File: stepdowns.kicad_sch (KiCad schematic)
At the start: 37 parts, among them J2 12V OUTLET, J3 5V OUTLET, U1 XL7005A, U2 ICW6215, U3 LM1117DT-3.3

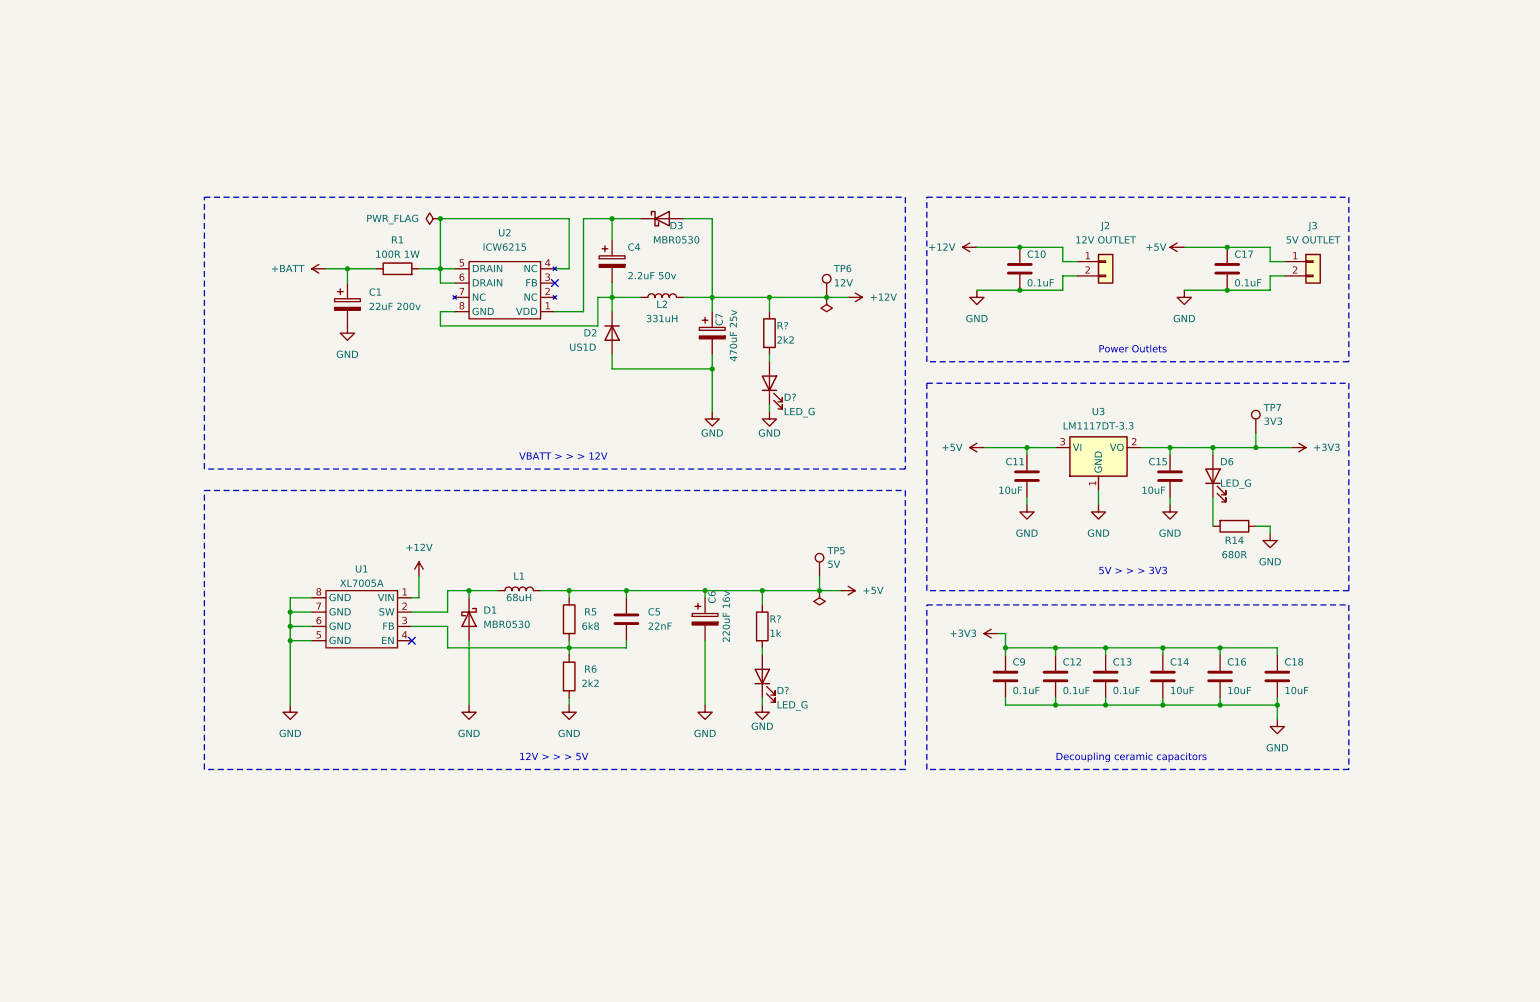
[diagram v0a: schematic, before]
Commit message: Add drivers, stepdown on VIPER115, fixes
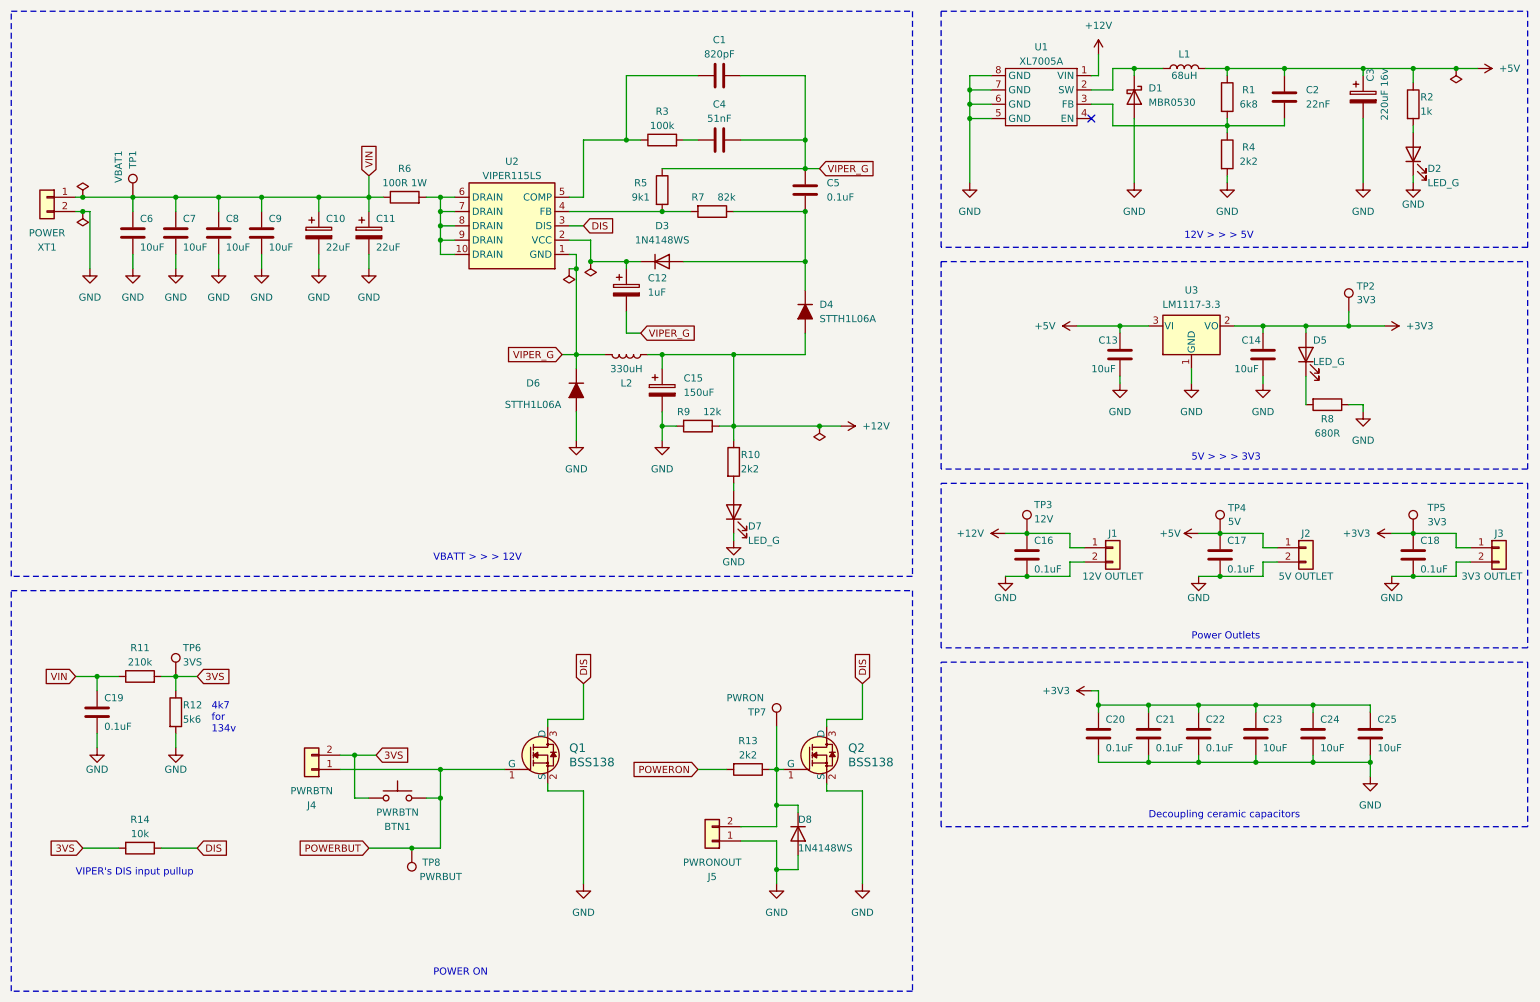
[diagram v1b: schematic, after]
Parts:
- removed C1: 22uF 200v, Capacitor_SMD:CP_Elec_10x10, symbol Device:C_Polarized
- removed C4: 2.2uF 50v, Capacitor_SMD:C_0805_2012Metric_Pad1.18x1.45mm_HandSolder, symbol Device:C_Polarized
- removed C7: 470uF 25v, Capacitor_SMD:CP_Elec_10x10.5, symbol Device:C_Polarized
- removed D2: US1D, Diode_SMD:D_SMA, symbol Diode:US1D
- removed D3: MBR0530, Diode_SMD:D_SOD-123, symbol Diode:MBR0530
- removed D?: LED_G, LED_SMD:LED_0603_1608Metric, symbol Device:LED
- removed R1: 100R 1W, Resistor_SMD:R_2010_5025Metric_Pad1.40x2.65mm_HandSolder, symbol Device:R
- removed R?: 2k2, Resistor_SMD:R_0603_1608Metric_Pad0.98x0.95mm_HandSolder, symbol Device:R
- removed U2: ICW6215, Package_SO:SOP-8_3.9x4.9mm_P1.27mm, symbol 4shift:ICW6215
- removed U3: LM1117DT-3.3, Package_TO_SOT_SMD:TO-252-3_TabPin2, symbol Regulator_Linear:LM1117DT-3.3
- added BTN1: PWRBTN, Button_Switch_SMD:SW_SPST_SKQG_WithoutStem, symbol Switch:SW_Push
- added C1: 820pF, Capacitor_SMD:C_0603_1608Metric_Pad1.08x0.95mm_HandSolder, symbol Device:C
- added C10, C11: 22uF, Capacitor_SMD:CP_Elec_10x10, symbol Device:C_Polarized
- added C12: 1uF, Capacitor_SMD:CP_Elec_10x10, symbol Device:C_Polarized
- added C15: 150uF, Capacitor_SMD:CP_Elec_10x10, symbol Device:C_Polarized
- added C18, C5: 0.1uF, Capacitor_SMD:C_0603_1608Metric_Pad1.08x0.95mm_HandSolder, symbol Device:C
- added C19: 0.1uF, Capacitor_SMD:C_0805_2012Metric_Pad1.18x1.45mm_HandSolder, symbol Device:C
- added C4: 51nF, Capacitor_SMD:C_0603_1608Metric_Pad1.08x0.95mm_HandSolder, symbol Device:C
- added C6, C7, C8, C9: 10uF, Capacitor_SMD:C_0603_1608Metric_Pad1.08x0.95mm_HandSolder, symbol Device:C
- added D3, D8: 1N4148WS, Diode_SMD:D_SOD-323, symbol Diode:1N4148WS
- added D4, D6: STTH1L06A, Diode_SMD:D_SMA_Handsoldering, symbol PCM_Diode_AKL:STTH1L06A
- added D7: LED_G, LED_SMD:LED_0603_1608Metric, symbol Device:LED
- added J3: 3V3 OUTLET, Connector_JST:JST_XH_B2B-XH-A_1x02_P2.50mm_Vertical, symbol Connector_Generic:Conn_01x02
- added J4: PWRBTN, Connector_JST:JST_XH_B2B-XH-A_1x02_P2.50mm_Vertical, symbol Connector_Generic:Conn_01x02
- added J5: PWRONOUT, Connector_JST:JST_XH_B2B-XH-A_1x02_P2.50mm_Vertical, symbol Connector_Generic:Conn_01x02
- added Q1, Q2: BSS138, digikey-footprints:SOT-23-3, symbol dk_Transistors-FETs-MOSFETs-Single:BSS138
- added R10, R13: 2k2, Resistor_SMD:R_0603_1608Metric_Pad0.98x0.95mm_HandSolder, symbol Device:R
- added R11: 210k, Resistor_SMD:R_0805_2012Metric_Pad1.20x1.40mm_HandSolder, symbol Device:R
- added R12: 5k6, Resistor_SMD:R_0805_2012Metric_Pad1.20x1.40mm_HandSolder, symbol Device:R
- added R14: 10k, Resistor_SMD:R_0603_1608Metric_Pad0.98x0.95mm_HandSolder, symbol Device:R
- added R3: 100k, Resistor_SMD:R_0201_0603Metric_Pad0.64x0.40mm_HandSolder, symbol Device:R
- added R5: 9k1, Resistor_SMD:R_0201_0603Metric_Pad0.64x0.40mm_HandSolder, symbol Device:R
- added R6: 100R 1W, Resistor_SMD:R_2010_5025Metric_Pad1.40x2.65mm_HandSolder, symbol Device:R
- added R7: 82k, Resistor_SMD:R_0201_0603Metric_Pad0.64x0.40mm_HandSolder, symbol Device:R
- added R9: 12k, Resistor_SMD:R_0201_0603Metric_Pad0.64x0.40mm_HandSolder, symbol Device:R
- added TP1: VBAT1, TestPoint:TestPoint_Pad_D2.0mm, symbol Connector:TestPoint
- added TP3: 12V, TestPoint:TestPoint_Pad_D2.0mm, symbol Connector:TestPoint
- added TP4: 5V, TestPoint:TestPoint_Pad_D2.0mm, symbol Connector:TestPoint
- added TP7: PWRON, TestPoint:TestPoint_Pad_D2.0mm, symbol Connector:TestPoint
- added TP8: PWRBUT, TestPoint:TestPoint_Pad_D2.0mm, symbol Connector:TestPoint
- added U2: VIPER115LS, 4shift:SOIC100P600X175-10N, symbol 4shift:VIPER115LSTR
- added U3: LM1117-3.3, Package_TO_SOT_SMD:SOT-223, symbol Regulator_Linear:LM1117-3.3
- added XT1: POWER, Connector_AMASS:AMASS_XT30PW-M_1x02_P2.50mm_Horizontal, symbol Connector_Generic:Conn_01x02
- J1: renamed from J2; footprint (none) -> Connector_JST:JST_XH_B2B-XH-A_1x02_P2.50mm_Vertical
- J2: renamed from J3; footprint (none) -> Connector_JST:JST_XH_B2B-XH-A_1x02_P2.50mm_Vertical
- L2: value 331uH -> 330uH
- TP5: value 5V -> 3V3
- TP6: value 12V -> 3VS
- gave numbers to parts that had none: 2
- renumbered C11 to C13, C15 to C14, C10 to C16, C5 to C2, C9 to C20, C12 to C21, C13 to C22, C14 to C23, C16 to C24, C18 to C25, C6 to C3, D6 to D5, R5 to R1, R6 to R4, R14 to R8, TP7 to TP2
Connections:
- net +12V: now also C15.1, D4.2 (A), R10.1, R9.1, TP3.1; no longer TP6.1
- net +3V3: now also TP5.1, C18.1, J3.1 (Pin_1), U3.2 (VO)
- net +5V: now also TP4.1, U3.3 (VI); no longer TP5.1
- net GND: now also C10.2, C11.2, C15.2, C18.2, C19.2, C6.2, C7.2, C8.2, C9.2, D6.2 (A), D7.1 (K), D8.2 (A), J3.2 (Pin_2), J5.1 (Pin_1), Q1.2 (S), Q2.2 (S), R12.2, R9.2, U3.1 (GND), XT1.2 (Pin_2)
- net VIPER_G: now reaches L2.1
- net VIPER_G: now also C1.2, C12.2, C4.2, C5.2, D6.1 (K), R5.1, U2.1 (GND)
- new net: R6.2, U2.10 (DRAIN), U2.6 (DRAIN), U2.7 (DRAIN), U2.8 (DRAIN), U2.9 (DRAIN)
- new net: D7.2 (A), R10.2
- new net: D8.1 (K), J5.2 (Pin_2), Q2.1 (G), R13.1, TP7.1
- new net: C12.1, D3.1 (K), U2.2 (VCC)
- new net: R5.2, R7.2, U2.4 (FB)
- new net: C1.1, R3.1, U2.5 (COMP)
- new net: C5.1, D3.2 (A), D4.1 (K), R7.1
- new net: C4.1, R3.2
- new net 3VS: BTN1.1, J4.2 (Pin_2), R11.2, R12.1, R14.2, TP6.1
- new net DIS: Q1.3 (D), Q2.3 (D), R14.1, U2.3 (DIS)
- new net POWERBUT: BTN1.2, J4.1 (Pin_1), Q1.1 (G), TP8.1
- new net POWERON: R13.2
- new net VIN: C10.1, C11.1, C19.1, C6.1, C7.1, C8.1, C9.1, R11.1, R6.1, TP1.1, XT1.1 (Pin_1)
- no-connect marks 2 -> 1
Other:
- note added: "4k7 for 134v"
- note added: "POWER ON"
- note added: "VIPER's DIS input pullup"
- moved on the sheet: C13, C14, C16, C17, C2, C20, C21, C22, C23, C24, C25, C3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

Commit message: topology in progress
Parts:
- C14: footprint Capacitor_SMD:C_0805_2012Metric -> Capacitor_SMD:C_0603_1608Metric_Pad1.08x0.95mm_HandSolder
- R3, R5, R7, R9: footprint Resistor_SMD:R_0201_0603Metric_Pad0.64x0.40mm_HandSolder -> Resistor_SMD:R_0603_1608Metric_Pad0.98x0.95mm_HandSolder
- R8: footprint Resistor_SMD:R_0402_1005Metric -> Resistor_SMD:R_0603_1608Metric_Pad0.98x0.95mm_HandSolder
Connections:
- net GND: now also XT1.1 (Pin_1); no longer XT1.2 (Pin_2)
- net VIN: now also XT1.2 (Pin_2); no longer XT1.1 (Pin_1)

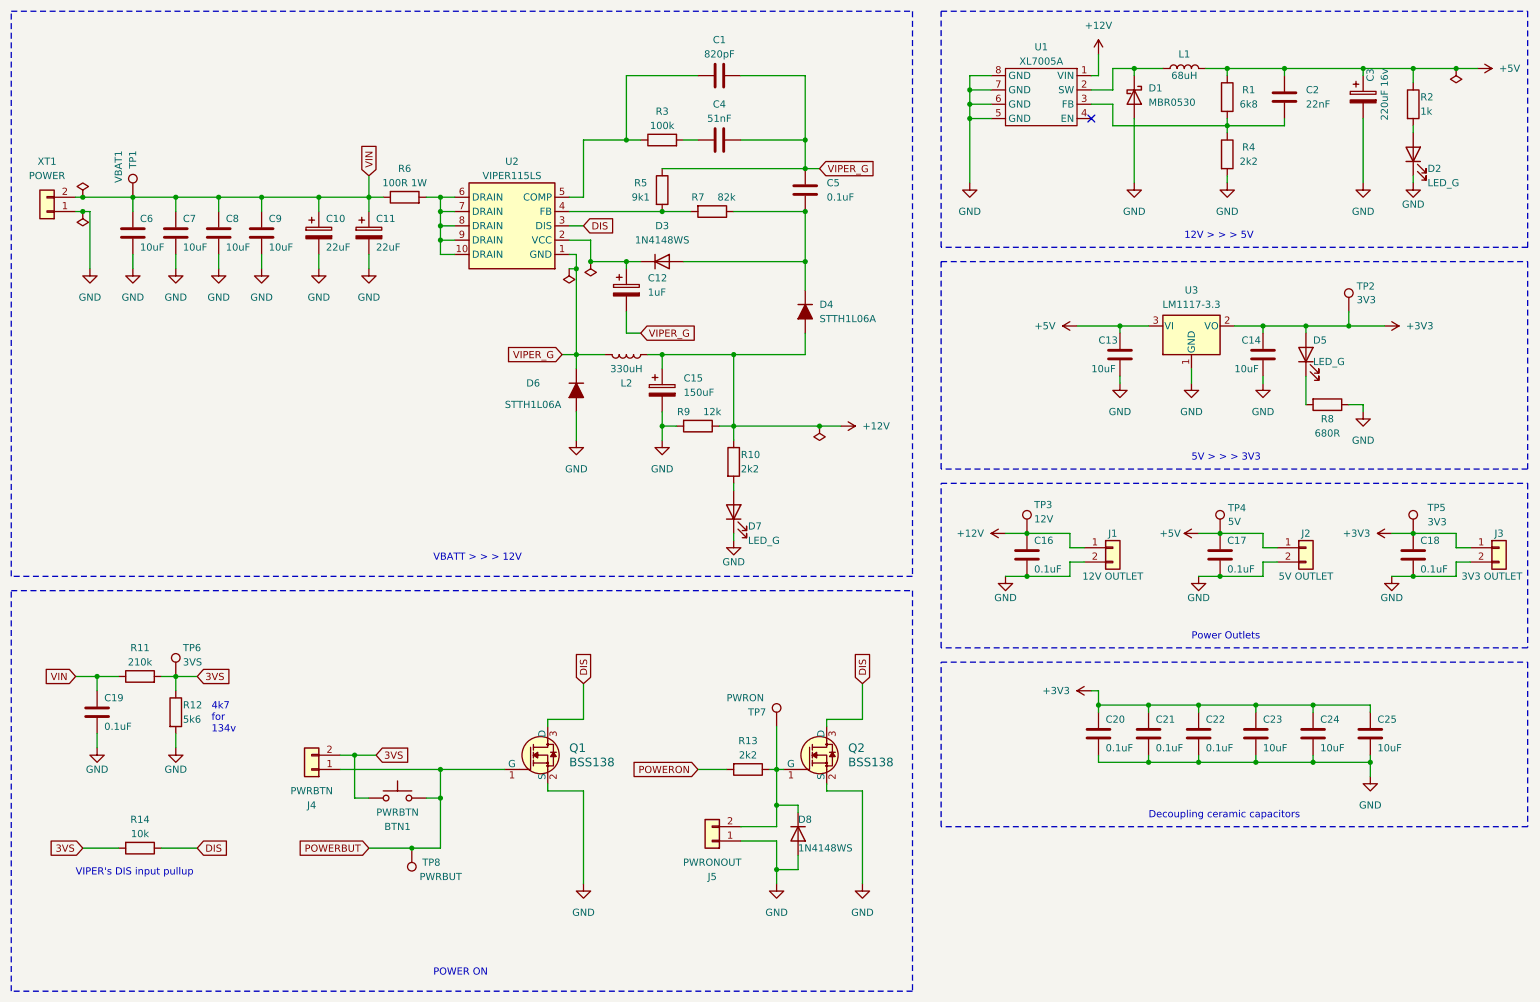
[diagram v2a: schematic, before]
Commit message: Replaced unused GPIO, added SWD connectorm, PCB in progress
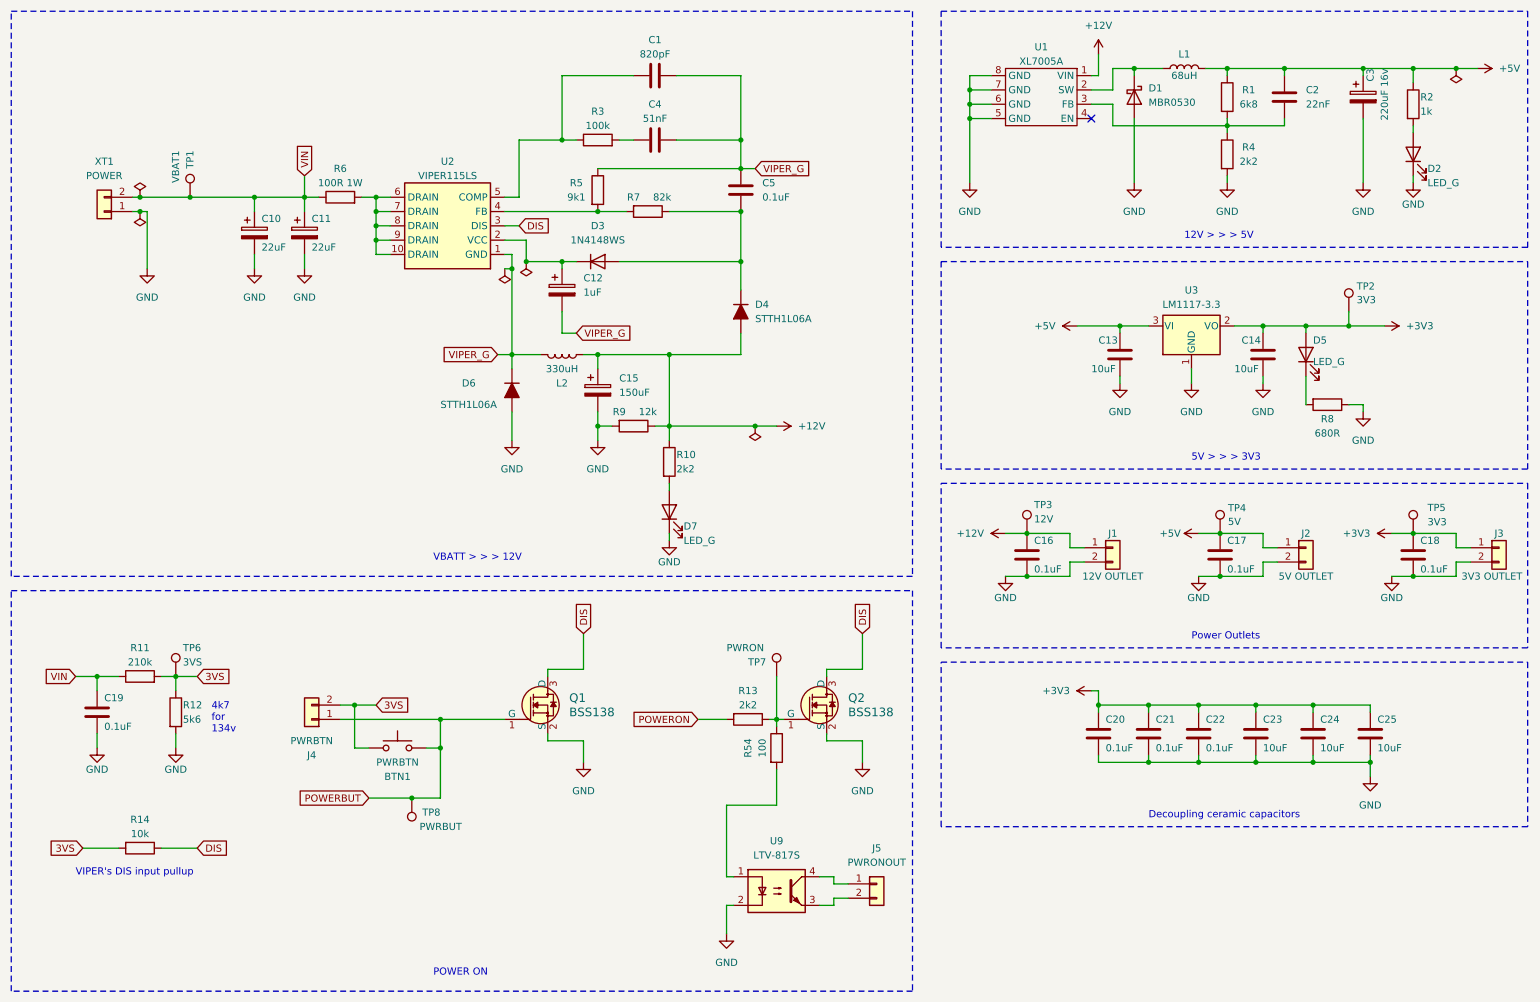
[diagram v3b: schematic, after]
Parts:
- removed C6, C7, C8, C9: 10uF, Capacitor_SMD:C_0603_1608Metric_Pad1.08x0.95mm_HandSolder, symbol Device:C
- removed D8: 1N4148WS, Diode_SMD:D_SOD-323, symbol Diode:1N4148WS
- added R54: 100, Resistor_SMD:R_0603_1608Metric_Pad0.98x0.95mm_HandSolder, symbol Device:R
- added U9: LTV-817S, Package_DIP:SMDIP-4_W9.53mm, symbol Isolator:LTV-817S
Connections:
- net GND: now also U9.2; no longer J5.1 (Pin_1)
- net at Q2.1 (G), R13.1, TP7.1: now also R54.1; no longer J5.2 (Pin_2)
- new net: R54.2, U9.1
- new net: J5.2 (Pin_2), U9.3
- new net: J5.1 (Pin_1), U9.4
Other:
- moved on the sheet: BTN1, C1, C10, C11, C12, C15, C4, C5, D3, D4, D6, D7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
